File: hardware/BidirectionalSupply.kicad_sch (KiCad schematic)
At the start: 0 parts

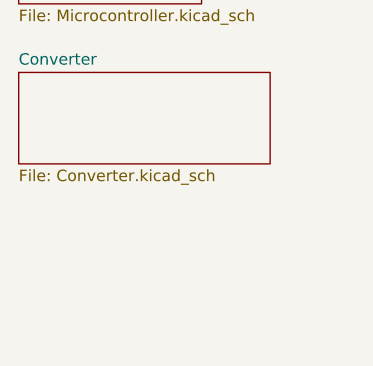
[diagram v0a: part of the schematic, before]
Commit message: WIP checkin * Added most of the JLCPCB part numbers * Added most of the component footprints * Connected up microcontroller and dc/dc converter
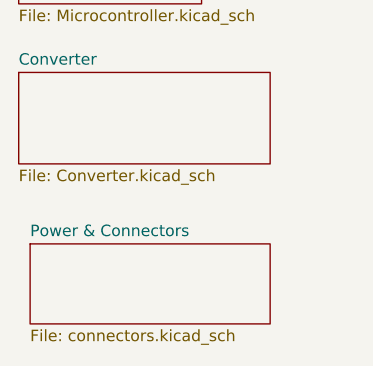
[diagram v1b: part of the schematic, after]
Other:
- added sheet Power & Connectors (connectors.kicad_sch)
- company: (none) -> Open Source Solutions Pty Ltd
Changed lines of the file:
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@@
 	(generator_version "8.0")
 	(paper "A4")
+	(title_block
+		(date "2025-11-07")
+		(rev "1.0")
+		(company "Open Source Solutions Pty Ltd")
+	)
 	(sheet
 		(at 36.83 33.02)
@@
 				)
 			)
+		)
+	)
+	(sheet
+		(at 38.1 68.58)
+		(size 26.67 8.89)
+		(fields_autoplaced yes)
+		(stroke
+			(width 0.1524)
+			(type solid)
+		)
+		(fill
+			(color 0 0 0 0.0000)
+		)
+		(property "Sheetname" "Power & Connectors"
+			(at 38.1 67.8684 0)
+			(effects
+				(font
+					(size 1.27 1.27)
+				)
+				(justify left bottom)
+			)
+		)
+		(property "Sheetfile" "connectors.kicad_sch"
+			(at 38.1 78.0546 0)
+			(effects
+				(font
+					(size 1.27 1.27)
+				)
+				(justify left top)
+			)
+		)
+		(instances
+			(project "BidirectionalSupply"
+				(path "/e5771ea0-f106-4b1c-9531-189f5725062b"
+					(page "4")
+				)
+			)

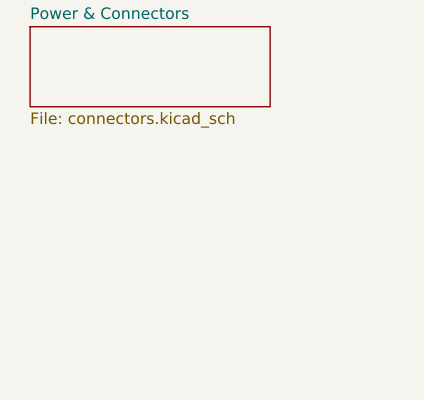
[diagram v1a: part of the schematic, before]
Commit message: Cleaned up share library Added switchmode 3v3 supply
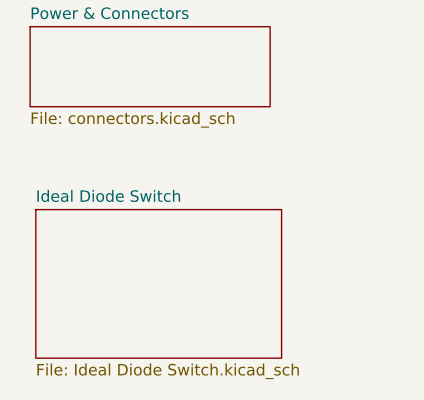
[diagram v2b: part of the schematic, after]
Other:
- added sheet Ideal Diode Switch (Ideal Diode Switch.kicad_sch)
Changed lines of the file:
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@@
+	)
+	(sheet
+		(at 38.735 88.9)
+		(size 27.305 16.51)
+		(fields_autoplaced yes)
+		(stroke
+			(width 0.1524)
+			(type solid)
+		)
+		(fill
+			(color 0 0 0 0.0000)
+		)
+		(property "Sheetname" "Ideal Diode Switch"
+			(at 38.735 88.1884 0)
+			(effects
+				(font
+					(size 1.27 1.27)
+				)
+				(justify left bottom)
+			)
+		)
+		(property "Sheetfile" "Ideal Diode Switch.kicad_sch"
+			(at 38.735 105.9946 0)
+			(effects
+				(font
+					(size 1.27 1.27)
+				)
+				(justify left top)
+			)
+		)
+		(instances
+			(project "BidirectionalSupply"
+				(path "/e5771ea0-f106-4b1c-9531-189f5725062b"
+					(page "5")
+				)
+			)
+		)
 	)
 	(sheet

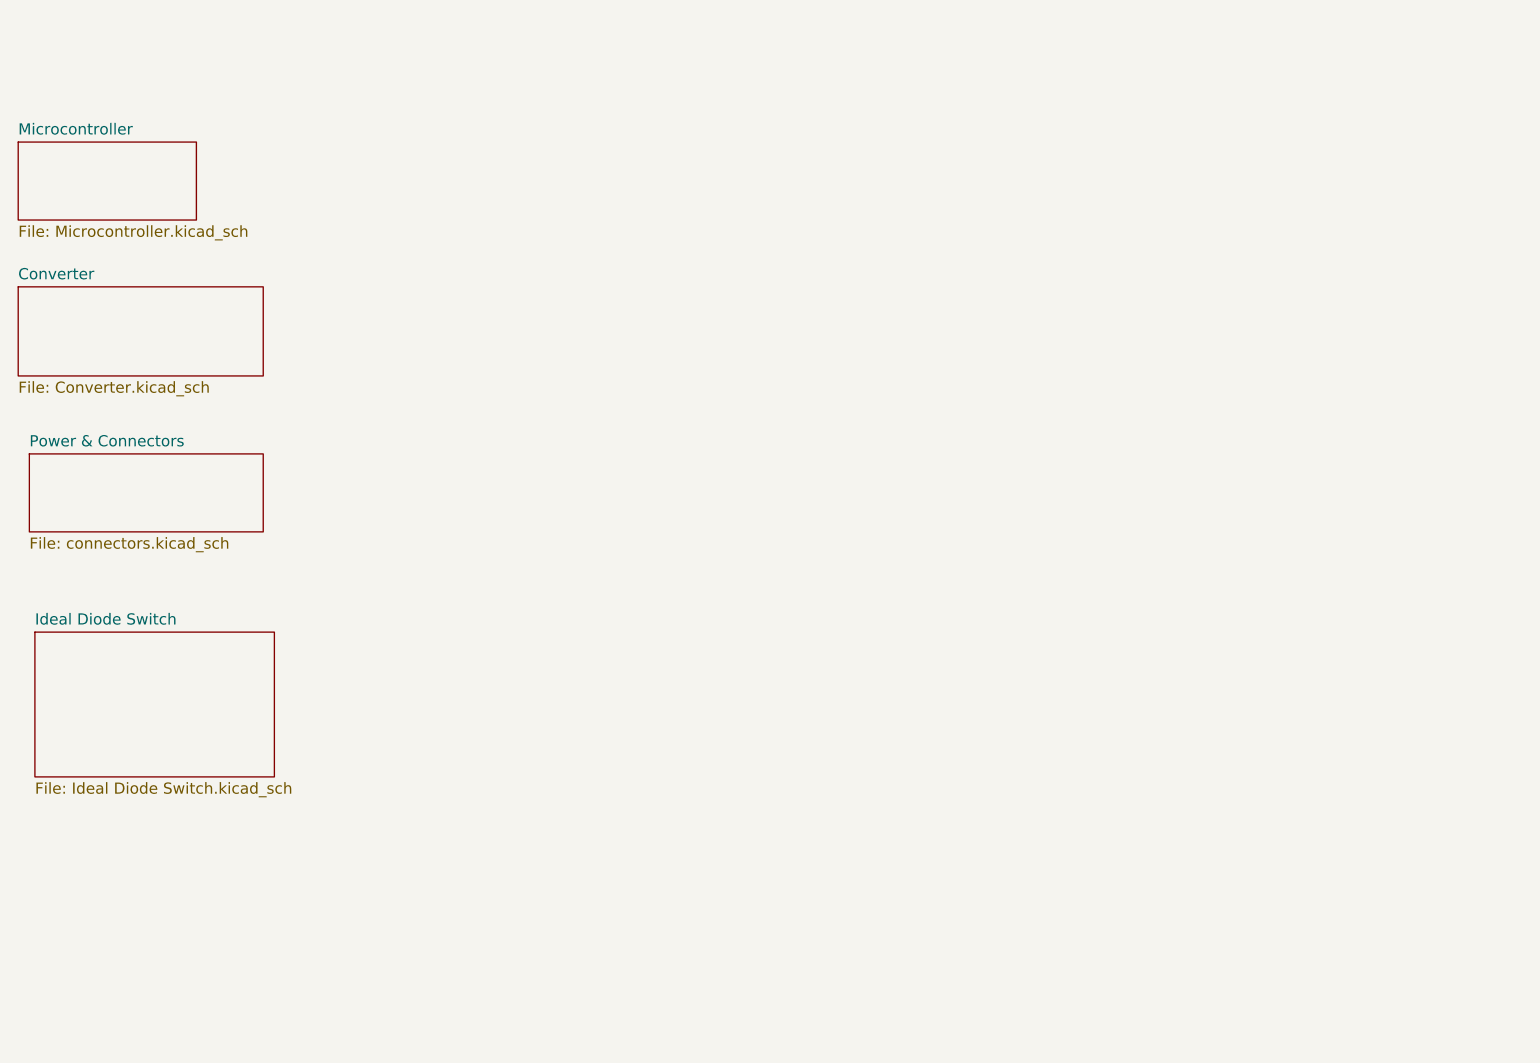
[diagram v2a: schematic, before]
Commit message: Added summary page Added prototyping area to PCB
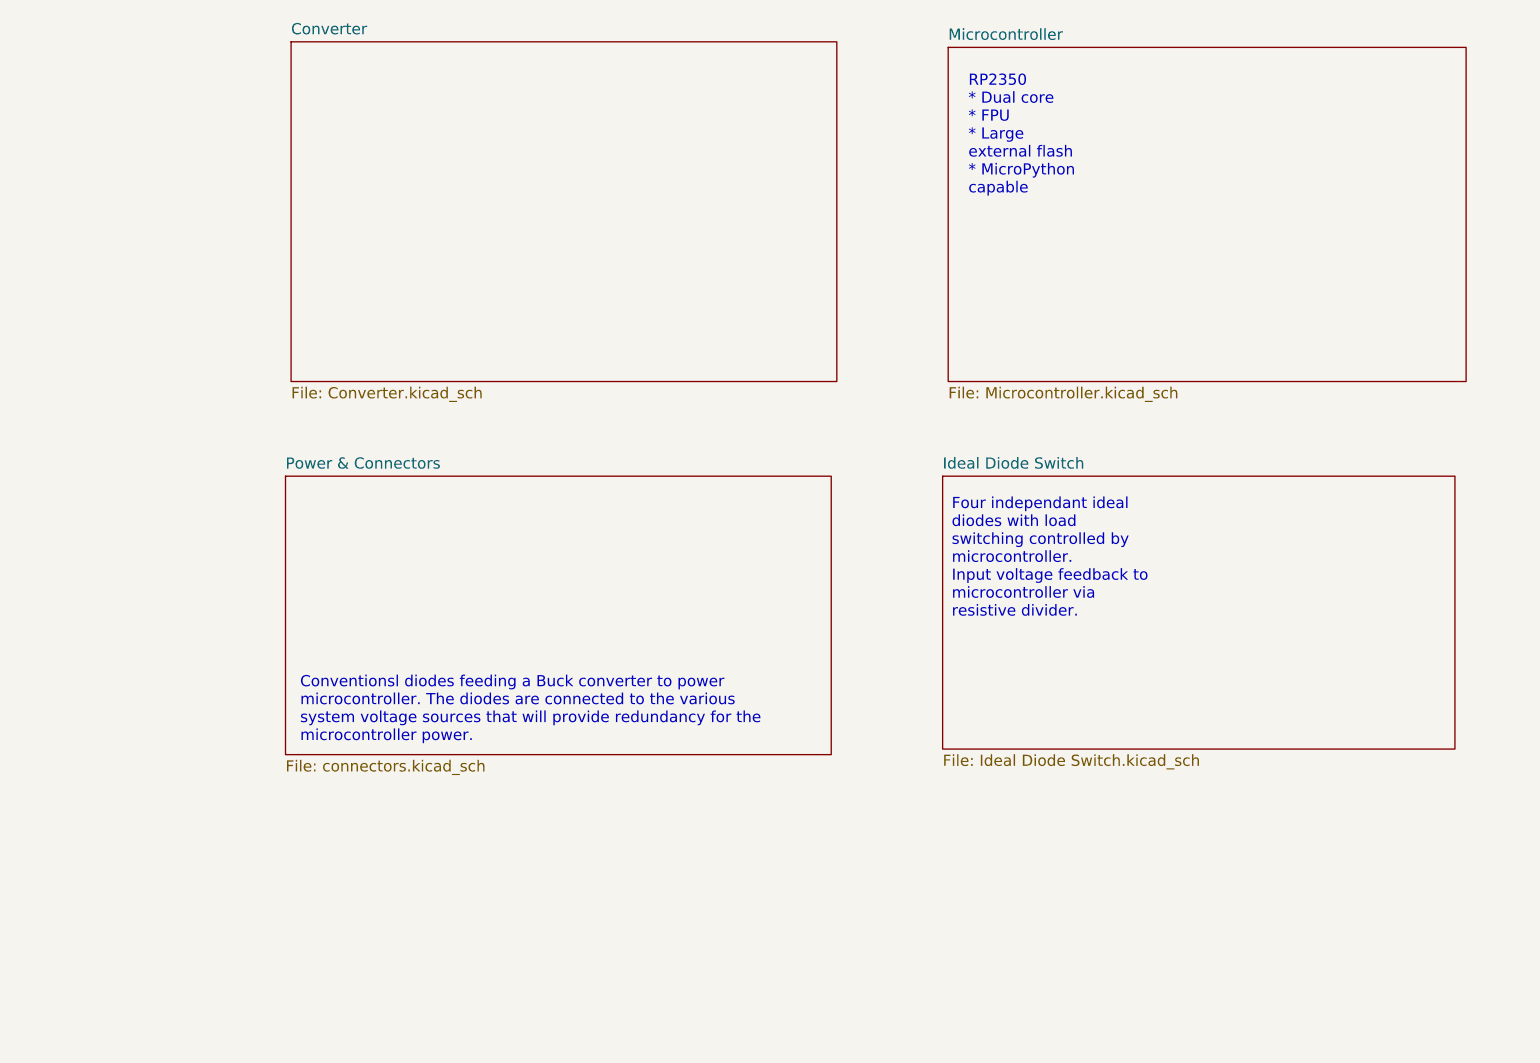
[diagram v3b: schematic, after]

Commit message: Ready for trial submit to JLCPCB
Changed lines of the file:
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@@
 	)
 	(image
-		(at 180.975 40.64)
+		(at 187.325 71.12)
 		(scale 0.786294)
 		(data "/9j/4Q/+RXhpZgAATU0AKgAAAAgABgESAAMAAAABAAEAAAEaAAUAAAABAAAAVgEbAAUAAAABAAAA"
@@
 	)
 	(image
-		(at 100.33 40.64)
+		(at 106.68 71.12)
 		(scale 0.629422)
 		(data "iVBORw0KGgoAAAANSUhEUgAAA+YAAAKoCAYAAAD6ReWPAAABJ2lDQ1BrQ0dDb2xvclNwYWNlQWRv"
@@
 	)
 	(image
-		(at 98.425 81.915)
+		(at 104.775 112.395)
 		(scale 0.287766)
 		(data "iVBORw0KGgoAAAANSUhEUgAAB9IAAANCCAYAAAA6LIcfAAABJ2lDQ1BrQ0dDb2xvclNwYWNlQWRv"
@@
 	)
 	(image
-		(at 184.785 84.455)
+		(at 191.135 114.935)
 		(scale 2.12927)
 		(data "/9j/4QDKRXhpZgAATU0AKgAAAAgABgESAAMAAAABAAEAAAEaAAUAAAABAAAAVgEbAAUAAAABAAAA"
@@
 	(text_box "RP2350\n* Dual core\n* FPU\n* Large external flash\n* MicroPython capable"
 		(exclude_from_sim no)
-		(at 144.145 24.13 0)
+		(at 150.495 54.61 0)
 		(size 17.78 15.24)
 		(stroke
@@
 	(text_box "Four independant ideal diodes with load switching controlled by microcontroller.\nInput voltage feedback to microcontroller via resistive divider."
 		(exclude_from_sim no)
-		(at 142.24 72.39 0)
+		(at 148.59 102.87 0)
 		(size 27.305 13.97)
 		(stroke
@@
 	(text_box "Conventionsl diodes feeding a Buck converter to power microcontroller. The diodes are connected to the various system voltage sources that will provide redundancy for the microcontroller power."
 		(exclude_from_sim no)
-		(at 67.945 92.71 0)
+		(at 74.295 123.19 0)
 		(size 61.595 9.525)
 		(stroke
@@
 	)
 	(sheet
-		(at 142.875 22.225)
+		(at 149.225 52.705)
 		(size 59.055 38.1)
 		(fields_autoplaced yes)
@@
 		)
 		(property "Sheetname" "Microcontroller"
-			(at 142.875 21.5134 0)
+			(at 149.225 51.9934 0)
 			(effects
 				(font
@@
 		)
 		(property "Sheetfile" "Microcontroller.kicad_sch"
-			(at 142.875 60.9096 0)
+			(at 149.225 91.3896 0)
 			(effects
 				(font
@@
 	)
 	(sheet
-		(at 142.24 71.12)
+		(at 148.59 101.6)
 		(size 58.42 31.115)
 		(fields_autoplaced yes)
@@
 		)
 		(property "Sheetname" "Ideal Diode Switch"
-			(at 142.24 70.4084 0)
+			(at 148.59 100.8884 0)
 			(effects
 				(font
@@
 		)
 		(property "Sheetfile" "Ideal Diode Switch.kicad_sch"
-			(at 142.24 102.8196 0)
+			(at 148.59 133.2996 0)
 			(effects
 				(font
@@
 	)
 	(sheet
-		(at 67.31 71.12)
+		(at 73.66 101.6)
 		(size 62.23 31.75)
 		(fields_autoplaced yes)
@@
 		)
 		(property "Sheetname" "Power & Connectors"
-			(at 67.31 70.4084 0)
+			(at 73.66 100.8884 0)
 			(effects
 				(font
@@
 		)
 		(property "Sheetfile" "connectors.kicad_sch"
-			(at 67.31 103.4546 0)
+			(at 73.66 133.9346 0)
 			(effects
 				(font
@@
 	)
 	(sheet
-		(at 67.945 21.59)
+		(at 74.295 52.07)
 		(size 62.23 38.735)
 		(fields_autoplaced yes)
@@
 		)
 		(property "Sheetname" "Converter"
-			(at 67.945 20.8784 0)
+			(at 74.295 51.3584 0)
 			(effects
 				(font
@@
 		)
 		(property "Sheetfile" "Converter.kicad_sch"
-			(at 67.945 60.9096 0)
+			(at 74.295 91.3896 0)
 			(effects
 				(font

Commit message: Update to the title block
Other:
- title: (none) -> Bidirectional Boost Buck Converter
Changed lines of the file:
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@@
 	(paper "A4")
 	(title_block
-		(date "2025-11-07")
+		(title "Bidirectional Boost Buck Converter")
+		(date "2025-11-24")
 		(rev "1.0")
 		(company "Open Source Solutions Pty Ltd")
